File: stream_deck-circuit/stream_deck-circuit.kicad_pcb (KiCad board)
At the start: 2 copper layers, 32 parts, among them SW10 SW_MEC_5G, SW11 SW_MEC_5G, SW12 SW_MEC_5G, SW13 SW_MEC_5G, SW14 SW_MEC_5G, SW15 SW_MEC_5G, SW16 SW_MEC_5G, SW17 SW_MEC_5G, SW3 SW_MEC_5G, SW4 SW_MEC_5G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

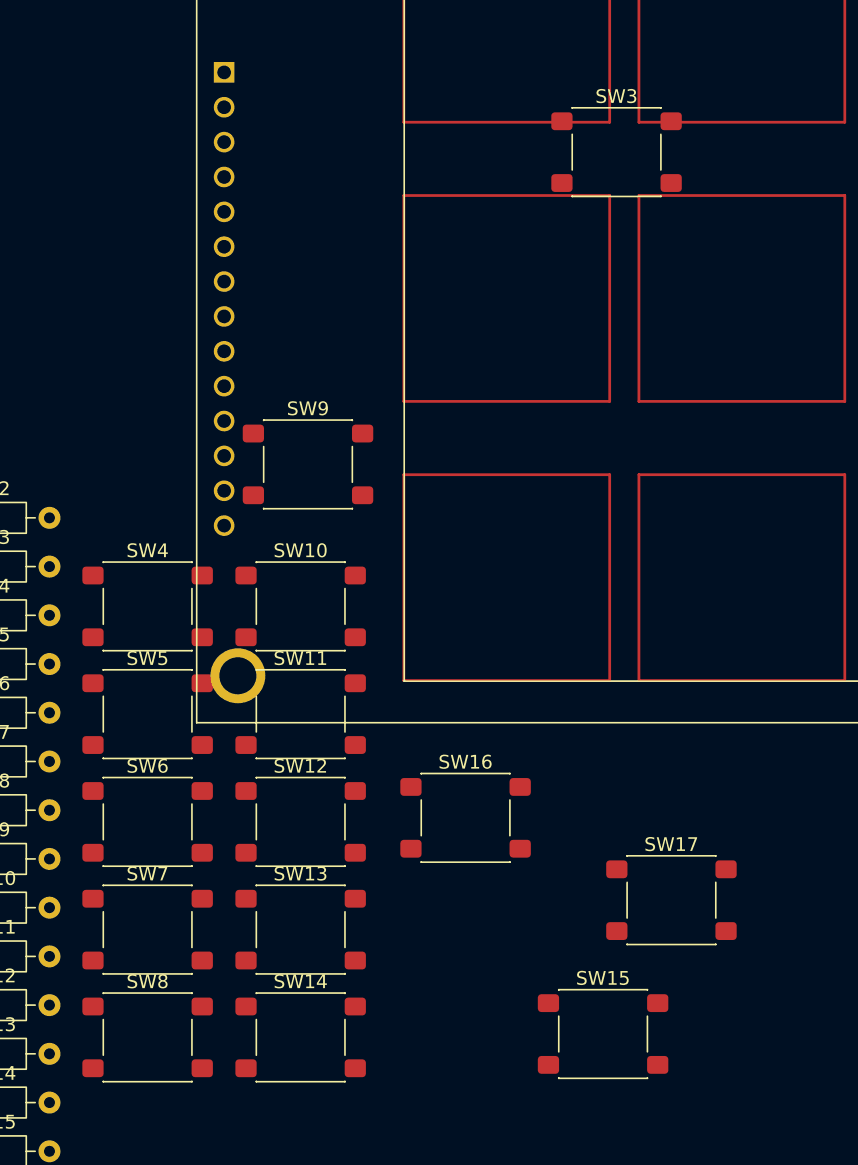
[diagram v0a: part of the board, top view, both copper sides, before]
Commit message: Update switch footprints in schematic and remove lock files
- Changed the footprint of multiple button switches from "Button_Switch_SMD:SW_SPST_PTS645Sx43SMTR92" to "Button_Switch_THT:SW_PUSH_1P1T_6x3.5mm_H5.0_APEM_MJTP1250" in the schematic file.
- Deleted lock files for the PCB, schematic, and project to ensure a clean working environment.

Signed-off-by: StrableD <89165077+strabled@users.noreply.github.com>
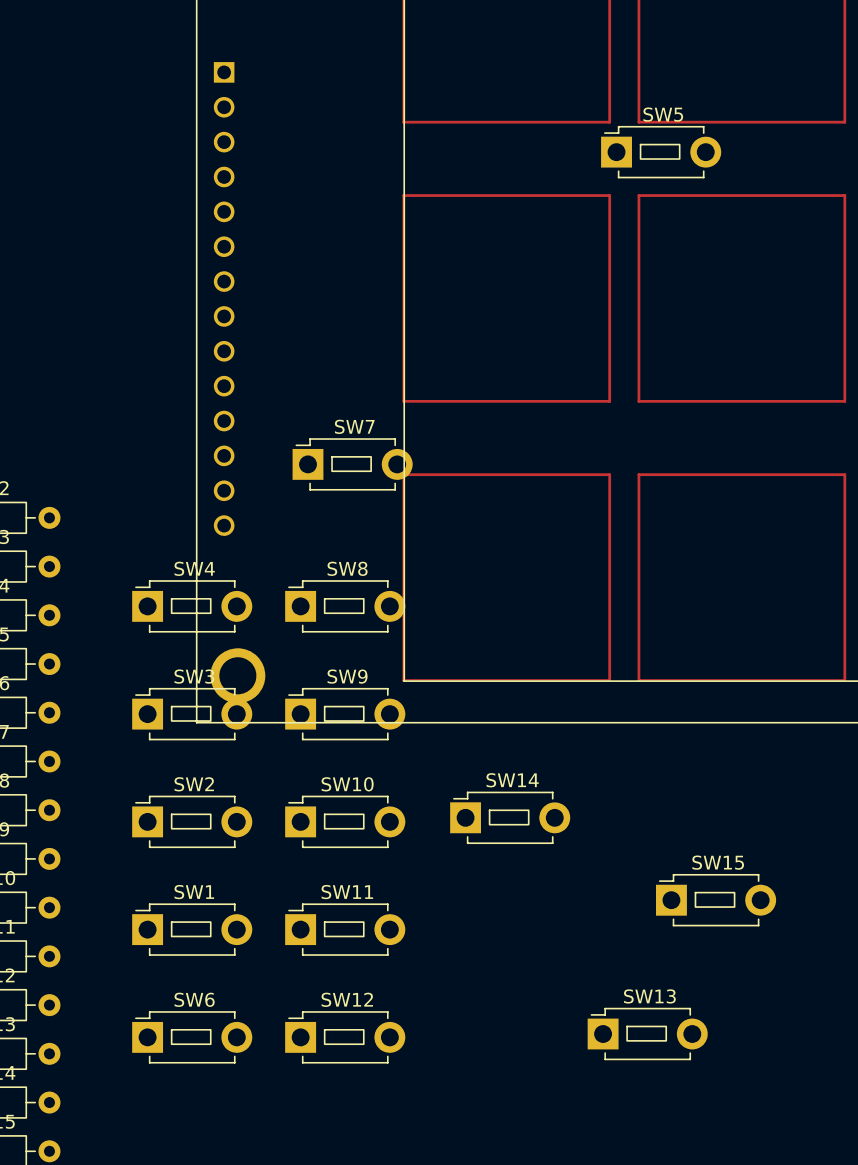
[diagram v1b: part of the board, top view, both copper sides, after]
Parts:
- SW1: renamed from SW7; footprint Button_Switch_SMD:SW_SPST_PTS645Sx43SMTR92 -> Button_Switch_THT:SW_PUSH_1P1T_6x3.5mm_H5.0_APEM_MJTP1250
- SW10: renamed from SW12; footprint Button_Switch_SMD:SW_SPST_PTS645Sx43SMTR92 -> Button_Switch_THT:SW_PUSH_1P1T_6x3.5mm_H5.0_APEM_MJTP1250
- SW11: renamed from SW13; footprint Button_Switch_SMD:SW_SPST_PTS645Sx43SMTR92 -> Button_Switch_THT:SW_PUSH_1P1T_6x3.5mm_H5.0_APEM_MJTP1250
- SW12: renamed from SW14; footprint Button_Switch_SMD:SW_SPST_PTS645Sx43SMTR92 -> Button_Switch_THT:SW_PUSH_1P1T_6x3.5mm_H5.0_APEM_MJTP1250
- SW13: renamed from SW15; footprint Button_Switch_SMD:SW_SPST_PTS645Sx43SMTR92 -> Button_Switch_THT:SW_PUSH_1P1T_6x3.5mm_H5.0_APEM_MJTP1250
- SW14: renamed from SW16; footprint Button_Switch_SMD:SW_SPST_PTS645Sx43SMTR92 -> Button_Switch_THT:SW_PUSH_1P1T_6x3.5mm_H5.0_APEM_MJTP1250
- SW15: renamed from SW17; footprint Button_Switch_SMD:SW_SPST_PTS645Sx43SMTR92 -> Button_Switch_THT:SW_PUSH_1P1T_6x3.5mm_H5.0_APEM_MJTP1250
- SW2: renamed from SW6; footprint Button_Switch_SMD:SW_SPST_PTS645Sx43SMTR92 -> Button_Switch_THT:SW_PUSH_1P1T_6x3.5mm_H5.0_APEM_MJTP1250
- SW3: renamed from SW5; footprint Button_Switch_SMD:SW_SPST_PTS645Sx43SMTR92 -> Button_Switch_THT:SW_PUSH_1P1T_6x3.5mm_H5.0_APEM_MJTP1250
- SW4: footprint Button_Switch_SMD:SW_SPST_PTS645Sx43SMTR92 -> Button_Switch_THT:SW_PUSH_1P1T_6x3.5mm_H5.0_APEM_MJTP1250
- SW5: renamed from SW3; footprint Button_Switch_SMD:SW_SPST_PTS645Sx43SMTR92 -> Button_Switch_THT:SW_PUSH_1P1T_6x3.5mm_H5.0_APEM_MJTP1250
- SW6: renamed from SW8; footprint Button_Switch_SMD:SW_SPST_PTS645Sx43SMTR92 -> Button_Switch_THT:SW_PUSH_1P1T_6x3.5mm_H5.0_APEM_MJTP1250
- SW7: renamed from SW9; footprint Button_Switch_SMD:SW_SPST_PTS645Sx43SMTR92 -> Button_Switch_THT:SW_PUSH_1P1T_6x3.5mm_H5.0_APEM_MJTP1250
- SW8: renamed from SW10; footprint Button_Switch_SMD:SW_SPST_PTS645Sx43SMTR92 -> Button_Switch_THT:SW_PUSH_1P1T_6x3.5mm_H5.0_APEM_MJTP1250
- SW9: renamed from SW11; footprint Button_Switch_SMD:SW_SPST_PTS645Sx43SMTR92 -> Button_Switch_THT:SW_PUSH_1P1T_6x3.5mm_H5.0_APEM_MJTP1250
